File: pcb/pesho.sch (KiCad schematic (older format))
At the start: 58 parts, among them IC1 4N25, IC2 4N25, IC3 4N25, IC4 4N25, IC5 4N25, IC6 4N25, P1 Power, P2 Bulkey, P3 Raspberry Pi CONN, P4 Serial, U1 JE-112D, U2 JE-112D, U3 JE-112D

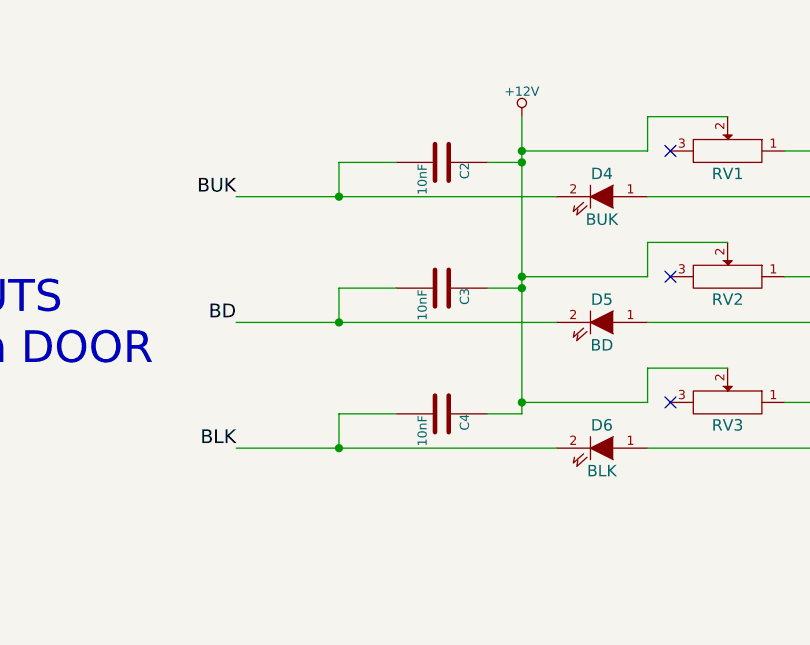
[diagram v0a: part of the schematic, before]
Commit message: better layout and all components on place
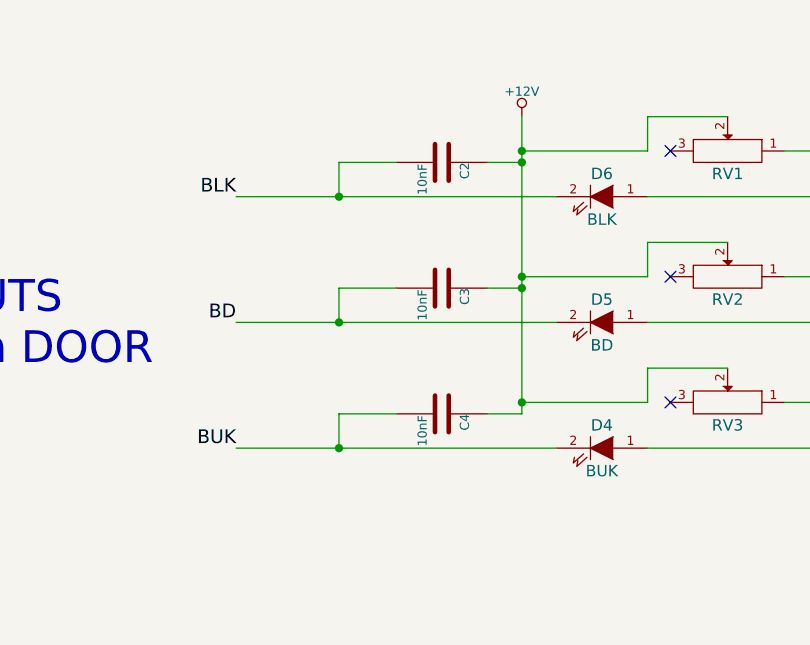
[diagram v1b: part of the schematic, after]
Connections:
- net BLK: now also C2.2; no longer C4.2
- net BUK: now also C4.2; no longer C2.2
- net at IC1.2: now also D6.1 (A); no longer D4.1 (A)
- net at IC3.2: now also D4.1 (A); no longer D6.1 (A)
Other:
- moved on the sheet: D4, D6
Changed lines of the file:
@@
 Text Label 14900 6650 1    60   ~ 0
 BUK
-Text Label 5650 5150 2    60   ~ 0
+Text Label 5650 4050 2    60   ~ 0
 BLK
 Text Label 5650 4600 2    60   ~ 0
 BD
-Text Label 5650 4050 2    60   ~ 0
+Text Label 5650 5150 2    60   ~ 0
 BUK
 $Comp
@@
 L LED D6
 U 1 1 54173522
-P 7250 5150
-F 0 "D6" H 7250 5250 50  0000 C CNN
-F 1 "BLK" H 7250 5050 50  0000 C CNN
-F 2 "led:LED-5MM" H 7250 5150 60  0001 C CNN
-F 3 "" H 7250 5150 60  0000 C CNN
-	1    7250 5150
+P 7250 4050
+F 0 "D6" H 7250 4150 50  0000 C CNN
+F 1 "BLK" H 7250 3950 50  0000 C CNN
+F 2 "led:LED-5MM" H 7250 4050 60  0001 C CNN
+F 3 "" H 7250 4050 60  0000 C CNN
+	1    7250 4050
 	-1   0    0    -1
 $EndComp
@@
 L LED D4
 U 1 1 54173C74
-P 7250 4050
-F 0 "D4" H 7250 4150 50  0000 C CNN
-F 1 "BUK" H 7250 3950 50  0000 C CNN
-F 2 "led:LED-5MM" H 7250 4050 60  0001 C CNN
-F 3 "" H 7250 4050 60  0000 C CNN
-	1    7250 4050
-	-1   0    0    -1
-$EndComp
+P 7250 5150
+F 0 "D4" H 7250 5250 50  0000 C CNN
+F 1 "BUK" H 7250 5050 50  0000 C CNN
+F 2 "led:LED-5MM" H 7250 5150 60  0001 C CNN
+F 3 "" H 7250 5150 60  0000 C CNN
+	1    7250 5150
+	-1   0    0    -1
+$EndComp

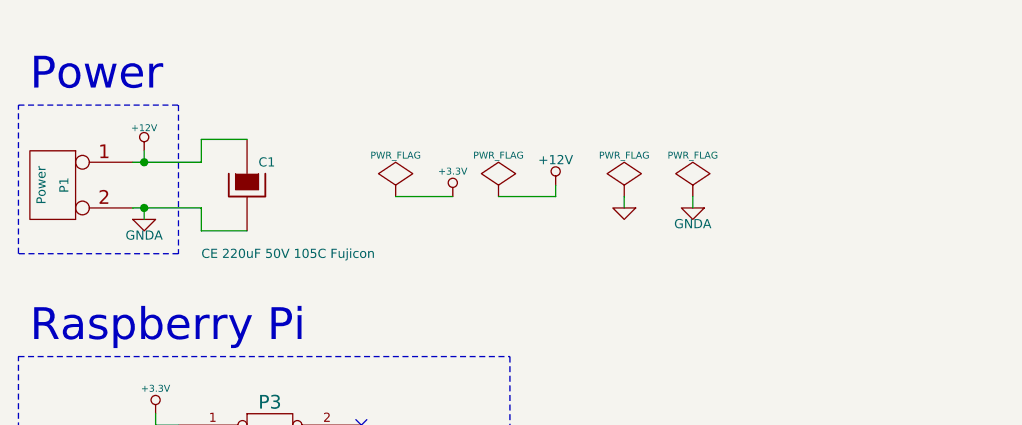
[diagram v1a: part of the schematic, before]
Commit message: 2 serial diodes added for protection.
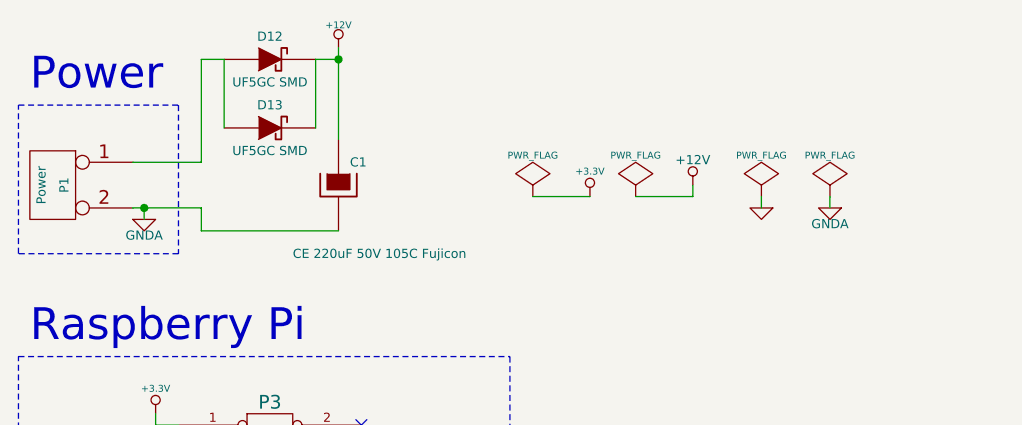
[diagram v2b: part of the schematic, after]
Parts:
- added D12, D13: UF5GC SMD, pesho:DO-214AB, symbol DIODESCH
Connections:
- net +12V: now also D12.2 (K), D13.2 (K); no longer P1.1 (P1)
- new net: D12.1 (A), D13.1 (A), P1.1 (P1)
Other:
- moved on the sheet: C1
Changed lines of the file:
@@
 L +12V #PWR013
 U 1 1 5416D74C
-P 1850 1350
-F 0 "#PWR013" H 1850 1300 20  0001 C CNN
-F 1 "+12V" H 1850 1450 30  0000 C CNN
-F 2 "" H 1850 1350 60  0000 C CNN
-F 3 "" H 1850 1350 60  0000 C CNN
-	1    1850 1350
+P 2700 900
+F 0 "#PWR013" H 2700 850 20  0001 C CNN
+F 1 "+12V" H 2700 1000 30  0000 C CNN
+F 2 "" H 2700 900 60  0000 C CNN
+F 3 "" H 2700 900 60  0000 C CNN
+	1    2700 900
 	1    0    0    -1
 $EndComp
@@
 L PWR_FLAG #FLG027
 U 1 1 5417F8F0
-P 3950 1550
-F 0 "#FLG027" H 3950 1645 30  0001 C CNN
-F 1 "PWR_FLAG" H 3950 1730 30  0000 C CNN
-F 2 "" H 3950 1550 60  0000 C CNN
-F 3 "" H 3950 1550 60  0000 C CNN
-	1    3950 1550
+P 4550 1550
+F 0 "#FLG027" H 4550 1645 30  0001 C CNN
+F 1 "PWR_FLAG" H 4550 1730 30  0000 C CNN
+F 2 "" H 4550 1550 60  0000 C CNN
+F 3 "" H 4550 1550 60  0000 C CNN
+	1    4550 1550
 	-1   0    0    -1
 $EndComp
@@
 L GND #PWR028
 U 1 1 5417FC74
-P 3950 1600
-F 0 "#PWR028" H 3950 1600 30  0001 C CNN
-F 1 "GND" H 3950 1530 30  0001 C CNN
-F 2 "" H 3950 1600 60  0000 C CNN
-F 3 "" H 3950 1600 60  0000 C CNN
-	1    3950 1600
+P 4550 1600
+F 0 "#PWR028" H 4550 1600 30  0001 C CNN
+F 1 "GND" H 4550 1530 30  0001 C CNN
+F 2 "" H 4550 1600 60  0000 C CNN
+F 3 "" H 4550 1600 60  0000 C CNN
+	1    4550 1600
 	-1   0    0    -1
 $EndComp
@@
 L +12V #PWR029
 U 1 1 54180887
-P 3650 1500
-F 0 "#PWR029" H 3650 1470 30  0001 C CNN
-F 1 "+12V" H 3650 1610 40  0000 C CNN
-F 2 "" H 3650 1500 60  0000 C CNN
-F 3 "" H 3650 1500 60  0000 C CNN
-	1    3650 1500
+P 4250 1500
+F 0 "#PWR029" H 4250 1470 30  0001 C CNN
+F 1 "+12V" H 4250 1610 40  0000 C CNN
+F 2 "" H 4250 1500 60  0000 C CNN
+F 3 "" H 4250 1500 60  0000 C CNN
+	1    4250 1500
 	-1   0    0    -1
 $EndComp
@@
 L PWR_FLAG #FLG030
 U 1 1 54180A4B
-P 3400 1550
-F 0 "#FLG030" H 3400 1645 30  0001 C CNN
-F 1 "PWR_FLAG" H 3400 1730 30  0000 C CNN
-F 2 "" H 3400 1550 60  0000 C CNN
-F 3 "" H 3400 1550 60  0000 C CNN
-	1    3400 1550
+P 4000 1550
+F 0 "#FLG030" H 4000 1645 30  0001 C CNN
+F 1 "PWR_FLAG" H 4000 1730 30  0000 C CNN
+F 2 "" H 4000 1550 60  0000 C CNN
+F 3 "" H 4000 1550 60  0000 C CNN
+	1    4000 1550
 	-1   0    0    -1
 $EndComp
@@
 L GNDA #PWR031
 U 1 1 54180F48
-P 4250 1600
-F 0 "#PWR031" H 4250 1600 40  0001 C CNN
-F 1 "GNDA" H 4250 1530 40  0000 C CNN
-F 2 "" H 4250 1600 60  0000 C CNN
-F 3 "" H 4250 1600 60  0000 C CNN
-	1    4250 1600
+P 4850 1600
+F 0 "#PWR031" H 4850 1600 40  0001 C CNN
+F 1 "GNDA" H 4850 1530 40  0000 C CNN
+F 2 "" H 4850 1600 60  0000 C CNN
+F 3 "" H 4850 1600 60  0000 C CNN
+	1    4850 1600
 	-1   0    0    -1
 $EndComp
@@
 L PWR_FLAG #FLG032
 U 1 1 54181178
-P 4250 1550
-F 0 "#FLG032" H 4250 1645 30  0001 C CNN
-F 1 "PWR_FLAG" H 4250 1730 30  0000 C CNN
-F 2 "" H 4250 1550 60  0000 C CNN
-F 3 "" H 4250 1550 60  0000 C CNN
-	1    4250 1550
+P 4850 1550
+F 0 "#FLG032" H 4850 1645 30  0001 C CNN
+F 1 "PWR_FLAG" H 4850 1730 30  0000 C CNN
+F 2 "" H 4850 1550 60  0000 C CNN
+F 3 "" H 4850 1550 60  0000 C CNN
+	1    4850 1550
 	-1   0    0    -1
 $EndComp
@@
 L PWR_FLAG #FLG033
 U 1 1 541821B1
-P 2950 1550
-F 0 "#FLG033" H 2950 1645 30  0001 C CNN
-F 1 "PWR_FLAG" H 2950 1730 30  0000 C CNN
-F 2 "" H 2950 1550 60  0000 C CNN
-F 3 "" H 2950 1550 60  0000 C CNN
-	1    2950 1550
+P 3550 1550
+F 0 "#FLG033" H 3550 1645 30  0001 C CNN
+F 1 "PWR_FLAG" H 3550 1730 30  0000 C CNN
+F 2 "" H 3550 1550 60  0000 C CNN
+F 3 "" H 3550 1550 60  0000 C CNN
+	1    3550 1550
 	-1   0    0    -1
 $EndComp
@@
 L +3.3V #PWR034
 U 1 1 541821ED
-P 3200 1550
-F 0 "#PWR034" H 3200 1510 30  0001 C CNN
-F 1 "+3.3V" H 3200 1660 30  0000 C CNN
-F 2 "" H 3200 1550 60  0000 C CNN
-F 3 "" H 3200 1550 60  0000 C CNN
-	1    3200 1550
+P 3800 1550
+F 0 "#PWR034" H 3800 1510 30  0001 C CNN
+F 1 "+3.3V" H 3800 1660 30  0000 C CNN
+F 2 "" H 3800 1550 60  0000 C CNN
+F 3 "" H 3800 1550 60  0000 C CNN
+	1    3800 1550
 	-1   0    0    -1
 $EndComp
@@
 	1800 1400 2100 1400
 Wire Wire Line
-	1850 1400 1850 1350
-Wire Wire Line
 	2000 2950 1900 2950
 Wire Wire Line
@@
 	3350 2900 3500 2900
 Wire Wire Line
-	3950 1550 3950 1600
-Wire Wire Line
-	3400 1550 3650 1550
-Wire Wire Line
-	3650 1550 3650 1500
-Wire Wire Line
-	4250 1550 4250 1600
-Wire Wire Line
-	2950 1550 3200 1550
+	4550 1550 4550 1600
+Wire Wire Line
+	4000 1550 4250 1550
+Wire Wire Line
+	4250 1550 4250 1500
+Wire Wire Line
+	4850 1550 4850 1600
+Wire Wire Line
+	3550 1550 3800 1550
 Wire Wire Line
 	7950 8100 8050 8100
@@
 L CAPAPOL C1
 U 1 1 5419B6A4
-P 2300 1500
-F 0 "C1" H 2350 1600 40  0000 L CNN
-F 1 "CE 220uF 50V 105C Fujicon" H 2100 1200 40  0000 L CNN
-F 2 "capacitors:CP_10x13mm" H 2400 1350 30  0001 C CNN
-F 3 "http://store.comet.bg/Catalogue/Product/4242/" H 2300 1500 300 0001 C CNN
-	1    2300 1500
-	1    0    0    -1
-$EndComp
-Wire Wire Line
-	2100 1400 2100 1300
-Wire Wire Line
-	2100 1300 2300 1300
-Connection ~ 1850 1400
+P 2700 1500
+F 0 "C1" H 2750 1600 40  0000 L CNN
+F 1 "CE 220uF 50V 105C Fujicon" H 2500 1200 40  0000 L CNN
+F 2 "capacitors:CP_10x13mm" H 2800 1350 30  0001 C CNN
+F 3 "http://store.comet.bg/Catalogue/Product/4242/" H 2700 1500 300 0001 C CNN
+	1    2700 1500
+	1    0    0    -1
+$EndComp
+Wire Wire Line
+	2100 1400 2100 950
+Wire Wire Line
+	2100 950  2200 950
 Wire Wire Line
 	2100 1600 2100 1700
 Wire Wire Line
-	2100 1700 2300 1700
+	2100 1700 2700 1700
 Connection ~ 1850 1600
 $Comp
@@
 Text Notes 11200 4550 0    139  ~ 0
 OUTPUT\nto Raspberry
+$Comp
+L DIODESCH D12
+U 1 1 542B0EC2
+P 2400 950
+F 0 "D12" H 2400 1050 40  0000 C CNN
+F 1 "UF5GC SMD" H 2400 850 40  0000 C CNN
+F 2 "pesho:DO-214AB" H 2400 950 60  0001 C CNN
+F 3 "http://store.comet.bg/download-file.php?id=5587" H 2400 950 60  0001 C CNN
+	1    2400 950
+	1    0    0    -1
+$EndComp
+Wire Wire Line
+	2350 1700 2350 1700
+Wire Wire Line
+	2200 950  2200 1250
+Wire Wire Line
+	2600 950  2600 1250
+Wire Wire Line
+	2600 950  2700 950
+Wire Wire Line
+	2700 900  2700 1300
+Connection ~ 2700 950
+$Comp
+L DIODESCH D13
+U 1 1 542B395E
+P 2400 1250
+F 0 "D13" H 2400 1350 40  0000 C CNN
+F 1 "UF5GC SMD" H 2400 1150 40  0000 C CNN
+F 2 "pesho:DO-214AB" H 2400 1250 60  0001 C CNN
+F 3 "http://store.comet.bg/download-file.php?id=5587" H 2400 1250 60  0001 C CNN
+	1    2400 1250
+	1    0    0    -1
+$EndComp
 $EndSCHEMATC

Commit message: Latest updates to the PCB included
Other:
- note added: "2 x 47 Ohms\nIN PARALLEL"
- note added: "DO NOT MOUNT\nD10 and D11"
- note added: "LAYOUT OF THE RELAYS IS FLIPPED !"
- note added: "RESISTORS CHANGED"
- note added: "SHORTED"
- note added: "SHOULD BE LEFT OPEN"
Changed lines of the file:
@@
 	0    1    1    0
 $EndComp
-Text Notes 7400 6650 0    60   ~ 0
+Text Notes 8050 6700 0    60   ~ 0
 3.3V / 5 mA
 $Comp
@@
 	1    0    0    -1
 $EndComp
+Text Notes 12900 6600 0    60   ~ 0
+DO NOT MOUNT\nD10 and D11
+Wire Notes Line
+	12900 7150 12400 7150
+Text Notes 12850 7100 0    60   ~ 0
+SHOULD BE LEFT OPEN
+Text Notes 9900 6800 0    60   ~ 0
+SHORTED
+Text Notes 9950 7300 0    60   ~ 0
+SHORTED
+Text Notes 9950 8150 0    60   ~ 0
+SHORTED
+Wire Notes Line
+	9850 6650 9600 6650
+Wire Notes Line
+	9600 6650 9600 6800
+Wire Notes Line
+	9850 7150 9600 7150
+Wire Notes Line
+	9600 7150 9600 7350
+Wire Notes Line
+	9850 7650 9600 7650
+Wire Notes Line
+	9600 7650 9600 7850
+Text Notes 10750 6050 0    60   ~ 0
+LAYOUT OF THE RELAYS IS FLIPPED !
+Text Notes 7350 7150 0    60   ~ 0
+2 x 47 Ohms\nIN PARALLEL
+Text Notes 7350 7650 0    60   ~ 0
+2 x 47 Ohms\nIN PARALLEL
+Text Notes 7300 8150 0    60   ~ 0
+2 x 47 Ohms\nIN PARALLEL
+Text Notes 6950 6700 0    60   ~ 0
+RESISTORS CHANGED
 $EndSCHEMATC

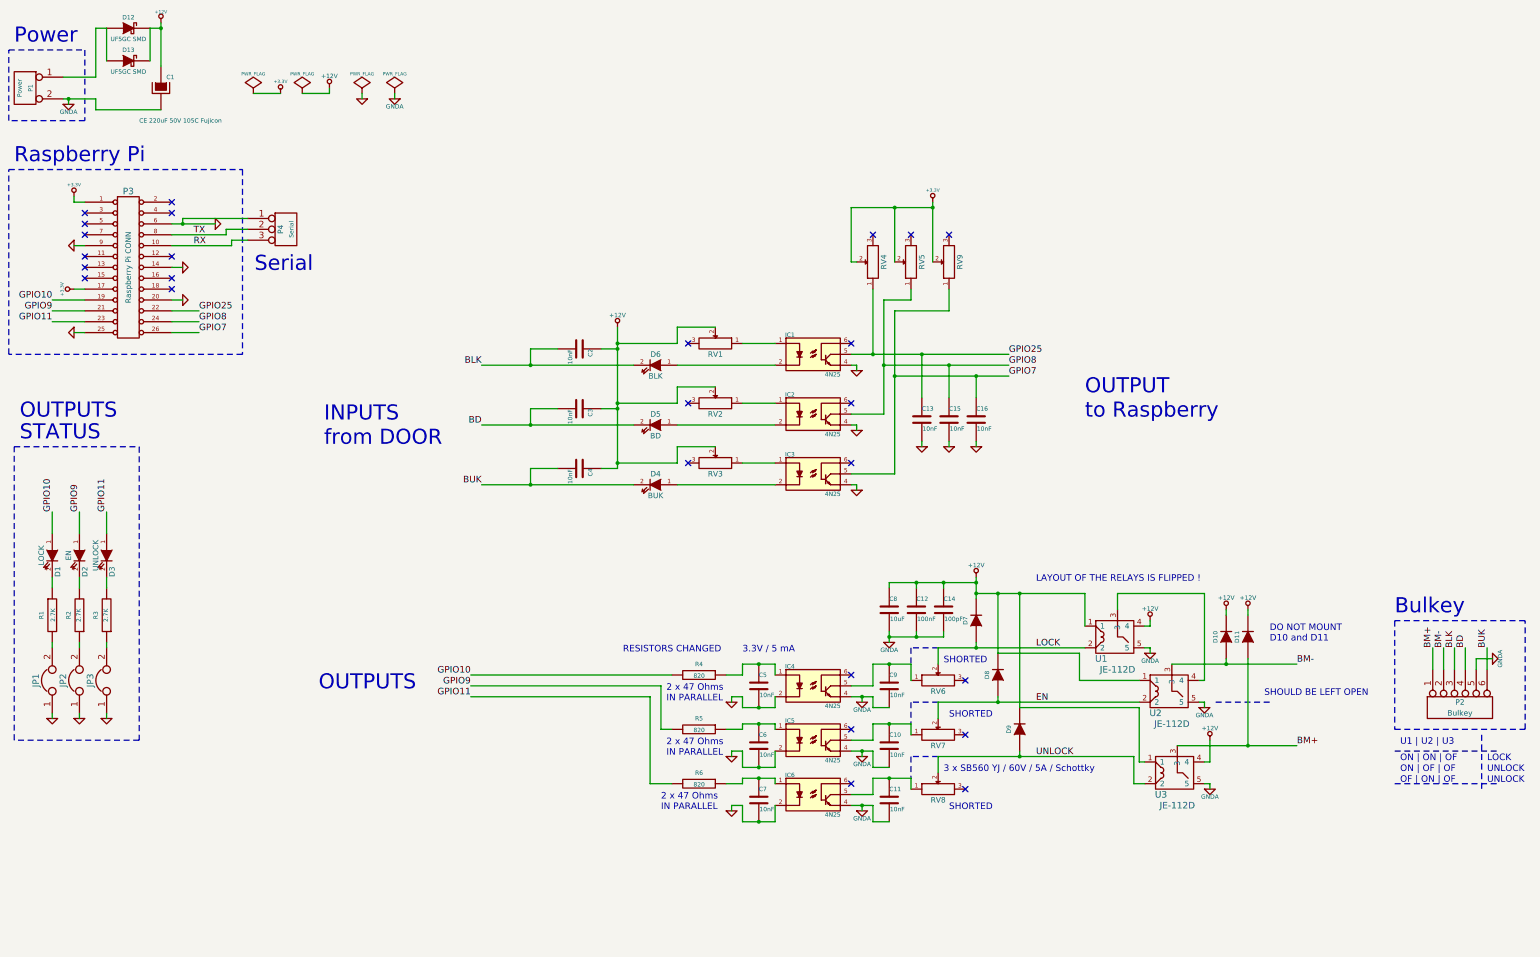
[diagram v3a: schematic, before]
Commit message: Schematic retought and resistor values changed.
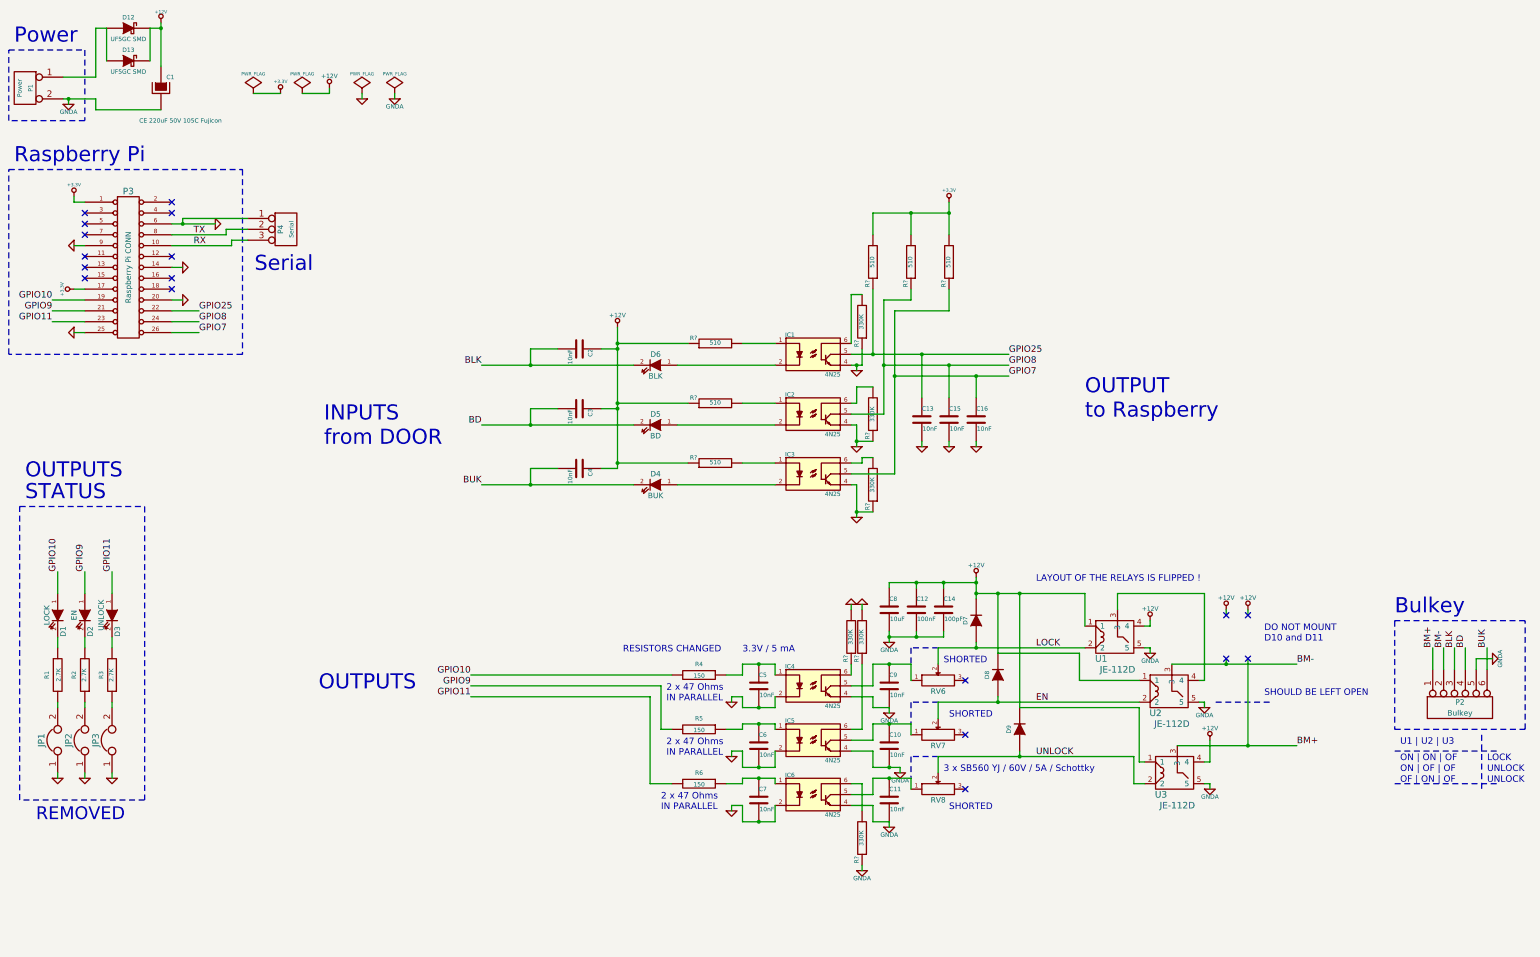
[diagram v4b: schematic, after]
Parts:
- removed D10, D11: SB560 YJ / 60V / 5A / Schottky, discret:D6.5, symbol DIODE
- removed RV1, RV2, RV3, RV4, RV5, RV9: 3296W(64W) 20K DIV, pesho:3968W, symbol POT
- added R? (x6): 330K, smd_capacitors:c_1206, symbol R
- added R? (x6): 510, smd_capacitors:c_1206, symbol R
- R4, R5, R6: value 820 -> 150
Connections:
- net +12V: now also R?.1, R?.1, R?.1
- net +3.3V: now also R?.2, R?.2, R?.2
- net GND: now also R?.1, R?.1, R?.1, R?.2, R?.2
- net GNDA: now also R?.1
- net GPIO25: now also R?.1
- net GPIO7: now also R?.1
- net GPIO8: now also R?.1
- net at IC1.1: now also R?.2
- net at IC1.6: now also R?.2
- net at IC2.1: now also R?.2
- net at IC2.6: now also R?.2
- net at IC3.1: now also R?.2
- net at IC3.6: now also R?.2
- net at IC6.6: now also R?.2
- net at IC5.6: now also R?.1
- net at IC4.6: now also R?.1
- no-connect marks 26 -> 18
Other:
- note added: "REMOVED"
- moved on the sheet: D1, D2, D3, JP1, JP2, JP3, R1, R2, R3
